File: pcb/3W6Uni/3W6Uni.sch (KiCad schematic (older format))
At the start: 91 parts, among them J1 USB_C Main, SW1 SW_Push, SW10 SW_Push, SW11 SW_Push, SW12 SW_Push, SW13 SW_Push, SW14 SW_Push, SW15 SW_Push, SW16 SW_Push, SW18 SW_Push, SW19 SW_Push, SW2 SW_Push, SW20 SW_Push, SW21 SW_Push, SW22 SW_Push, SW23 SW_Push, SW24 SW_Push, SW25 SW_Push, SW26 SW_Push, SW27 SW_Push, SW28 SW_Push, SW29 SW_Push, SW3 SW_Push, SW30 SW_Push, SW31 SW_Push, SW32 SW_Push, SW33 SW_Push, SW34 SW_Push, SW35 SW_Push, SW36 SW_Push, SW37 SW_Push, SW4 SW_Push, SW5 SW_Push, SW6 SW_Push, SW7 SW_Push, SW8 SW_Push, SW9 SW_Push, U1 ATmega32U4-AU, Y1 16MHZ

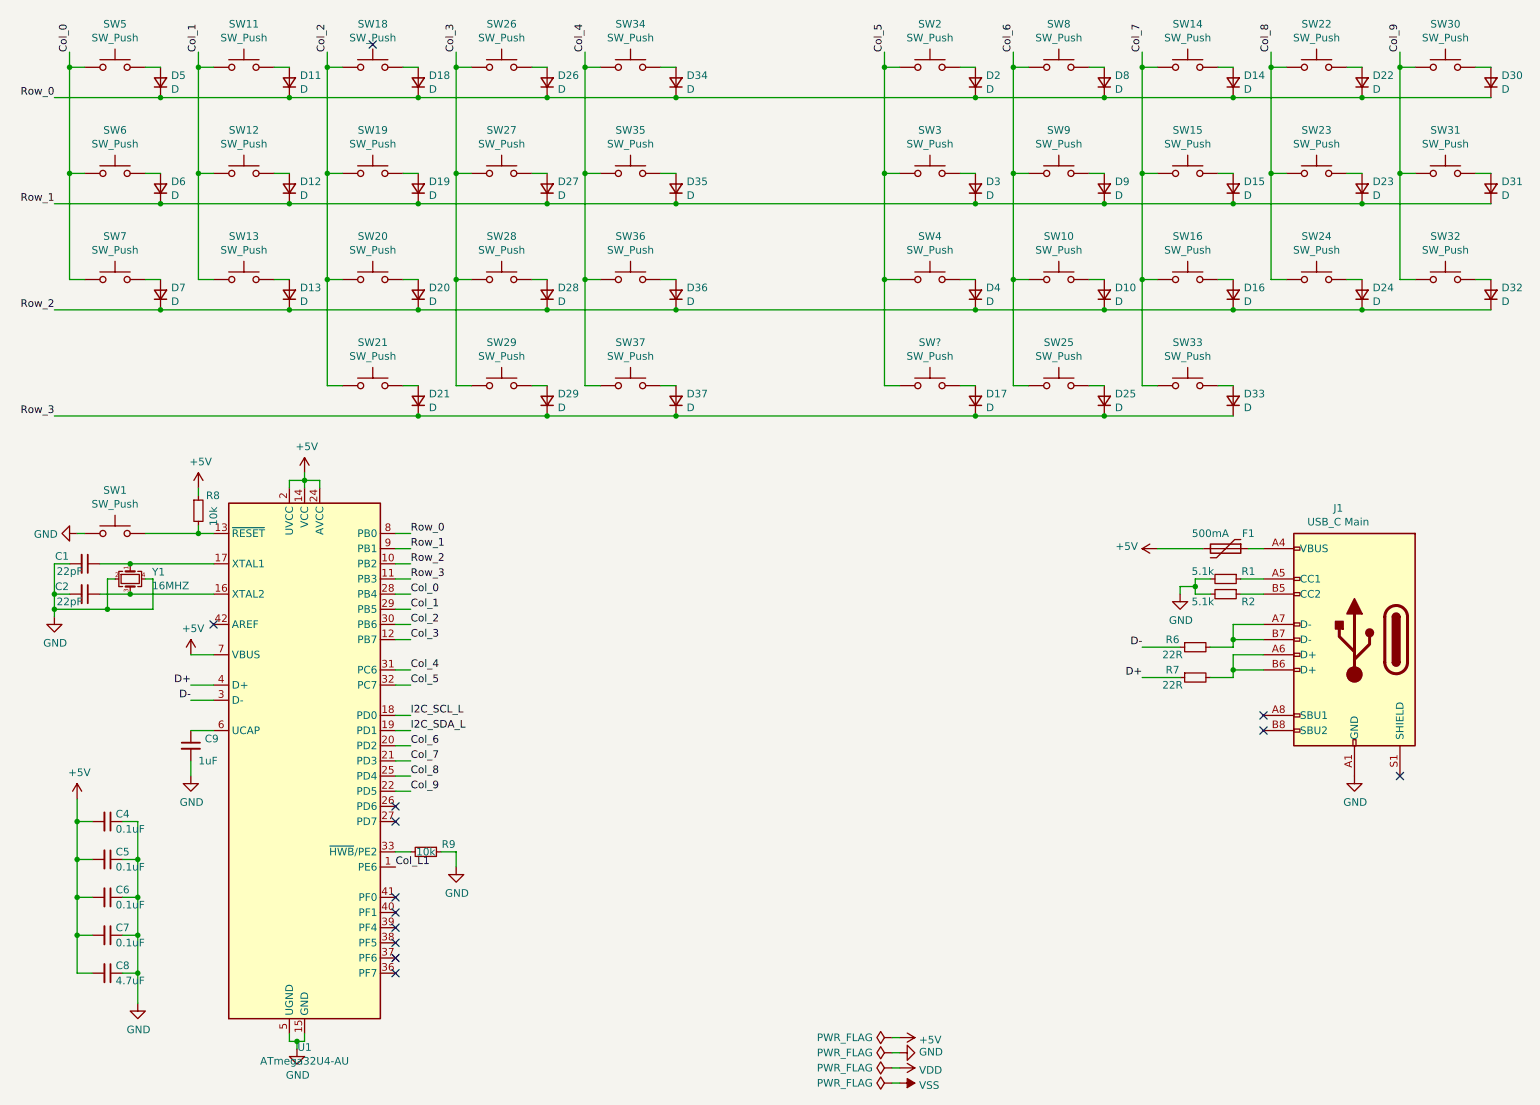
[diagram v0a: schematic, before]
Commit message: add rotary encoder to lib.WIP PCB
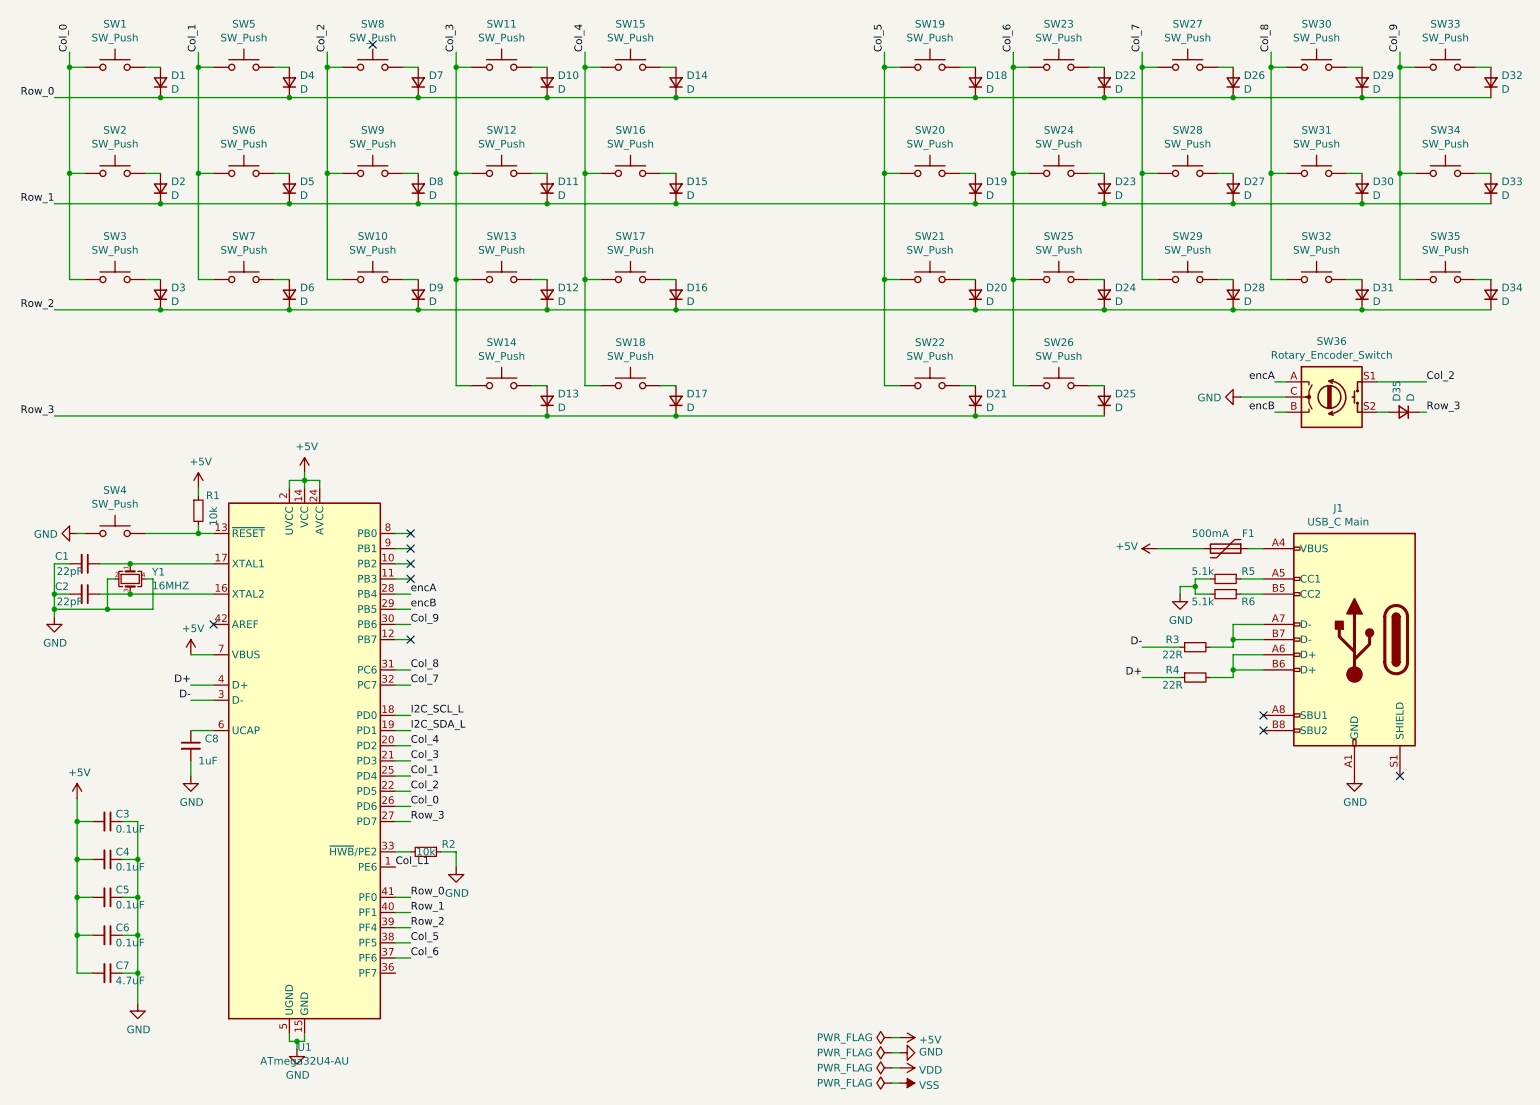
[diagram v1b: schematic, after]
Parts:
- removed D21, D33: D, Weteor:D_SOD-123, symbol Device:D_Small
- removed SW21, SW?: SW_Push, Weteor:Kailh_Choc_1u, symbol Switch:SW_Push
- added D35: D, Weteor:D_SOD-123, symbol Device:D_Small
- added SW36: Rotary_Encoder_Switch, Weteor:RotEncoderE11, symbol Device:Rotary_Encoder_Switch
- C1, C2: footprint Weteor:C_0402_HandSolder -> Capacitor_SMD:C_0805_2012Metric_Pad1.18x1.45mm_HandSolder
- C3: renamed from C4; footprint Weteor:C_0402_HandSolder -> Capacitor_SMD:C_0805_2012Metric_Pad1.18x1.45mm_HandSolder
- C4: renamed from C5; footprint Weteor:C_0402_HandSolder -> Capacitor_SMD:C_0805_2012Metric_Pad1.18x1.45mm_HandSolder
- C5: renamed from C6; footprint Weteor:C_0402_HandSolder -> Capacitor_SMD:C_0805_2012Metric_Pad1.18x1.45mm_HandSolder
- C6: renamed from C7; footprint Weteor:C_0402_HandSolder -> Capacitor_SMD:C_0805_2012Metric_Pad1.18x1.45mm_HandSolder
- C7: renamed from C8; footprint Weteor:C_0402_HandSolder -> Capacitor_SMD:C_0805_2012Metric_Pad1.18x1.45mm_HandSolder
- C8: renamed from C9; footprint Weteor:C_0402_HandSolder -> Capacitor_SMD:C_0805_2012Metric_Pad1.18x1.45mm_HandSolder
- R1: renamed from R8; footprint Weteor:R_0402_HandSolder -> Resistor_SMD:R_0805_2012Metric_Pad1.20x1.40mm_HandSolder
- R2: renamed from R9; footprint Weteor:R_0402_HandSolder -> Resistor_SMD:R_0805_2012Metric_Pad1.20x1.40mm_HandSolder
- R3: renamed from R6; footprint Weteor:R_0402_HandSolder -> Resistor_SMD:R_0805_2012Metric_Pad1.20x1.40mm_HandSolder
- R4: renamed from R7; footprint Weteor:R_0402_HandSolder -> Resistor_SMD:R_0805_2012Metric_Pad1.20x1.40mm_HandSolder
- R5: renamed from R1; footprint Weteor:R_0402_HandSolder -> Resistor_SMD:R_0805_2012Metric_Pad1.20x1.40mm_HandSolder
- R6: renamed from R2; footprint Weteor:R_0402_HandSolder -> Resistor_SMD:R_0805_2012Metric_Pad1.20x1.40mm_HandSolder
- renumbered D5 to D1, D26 to D10, D27 to D11, D28 to D12, D29 to D13, D34 to D14, D35 to D15, D36 to D16, D37 to D17, D2 to D18, D3 to D19, D6 to D2, D4 to D20, D17 to D21, D8 to D22, D9 to D23, D10 to D24, D14 to D26, D15 to D27, D16 to D28, D22 to D29, D7 to D3, D23 to D30, D24 to D31, D30 to D32, D31 to D33, D32 to D34, D11 to D4, D12 to D5, D13 to D6, D18 to D7, D19 to D8, D20 to D9, SW5 to SW1, SW20 to SW10, SW26 to SW11, SW27 to SW12, SW28 to SW13, SW37 to SW14, SW34 to SW15, SW35 to SW16, SW36 to SW17, SW29 to SW18, SW2 to SW19, SW6 to SW2, SW3 to SW20, SW4 to SW21, SW25 to SW22, SW8 to SW23, SW9 to SW24, SW10 to SW25, SW33 to SW26, SW14 to SW27, SW15 to SW28, SW16 to SW29, SW7 to SW3, SW22 to SW30, SW23 to SW31, SW24 to SW32, SW30 to SW33, SW31 to SW34, SW32 to SW35, SW1 to SW4, SW11 to SW5, SW12 to SW6, SW13 to SW7, SW18 to SW8, SW19 to SW9
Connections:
- net Col_0: now also U1.26 (PD6); no longer U1.28 (PB4)
- net Col_1: now also U1.25 (PD4); no longer U1.29 (PB5)
- net Col_2: now also U1.22 (PD5), SW36.S1; no longer U1.30 (PB6)
- net Col_3: now also SW14.1, U1.21 (PD3); no longer SW18.1, U1.12 (PB7)
- net Col_4: now also SW18.1, U1.20 (PD2); no longer SW14.1, U1.31 (PC6)
- net Col_5: now also SW22.1, U1.38 (PF5); no longer U1.32 (PC7)
- net Col_6: now also SW26.1, U1.37 (PF6); no longer SW22.1, U1.20 (PD2)
- net Col_7: now also U1.32 (PC7); no longer SW26.1, U1.21 (PD3)
- net Col_8: now also U1.31 (PC6); no longer U1.25 (PD4)
- net Col_9: now also U1.30 (PB6); no longer U1.22 (PD5)
- net GND: now also SW36.C
- net Row_0: now also U1.41 (PF0); no longer U1.8 (PB0)
- net Row_1: now also U1.40 (PF1); no longer U1.9 (PB1)
- net Row_2: now also U1.39 (PF4); no longer U1.10 (PB2)
- net Row_3: now also U1.27 (PD7), D35.1 (K); no longer U1.11 (PB3)
- net at SW18.2: now also D17.2 (A); no longer D13.2 (A)
- net at SW14.2: now also D13.2 (A); no longer D17.2 (A)
- net at SW22.2: now also D21.2 (A); no longer D25.2 (A)
- net at SW26.2: now also D25.2 (A)
- new net: D35.2 (A), SW36.S2
- new net encA: SW36.A, U1.28 (PB4)
- new net encB: SW36.B, U1.29 (PB5)
- no-connect marks 13 -> 10
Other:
- moved on the sheet: SW14, SW18, SW22, SW26
